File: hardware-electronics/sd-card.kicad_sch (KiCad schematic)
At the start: 48 parts, among them J5 Micro_SD_Card_Det_Hirose_DM3AT, J8 TC2030-IDC-NL, Q6 BSS138, Q7 BSS138, U6 24AA04T-I_OT, U9 USB2244-AEZG-06, Y3 ECS-240-10-47-CKM-TR

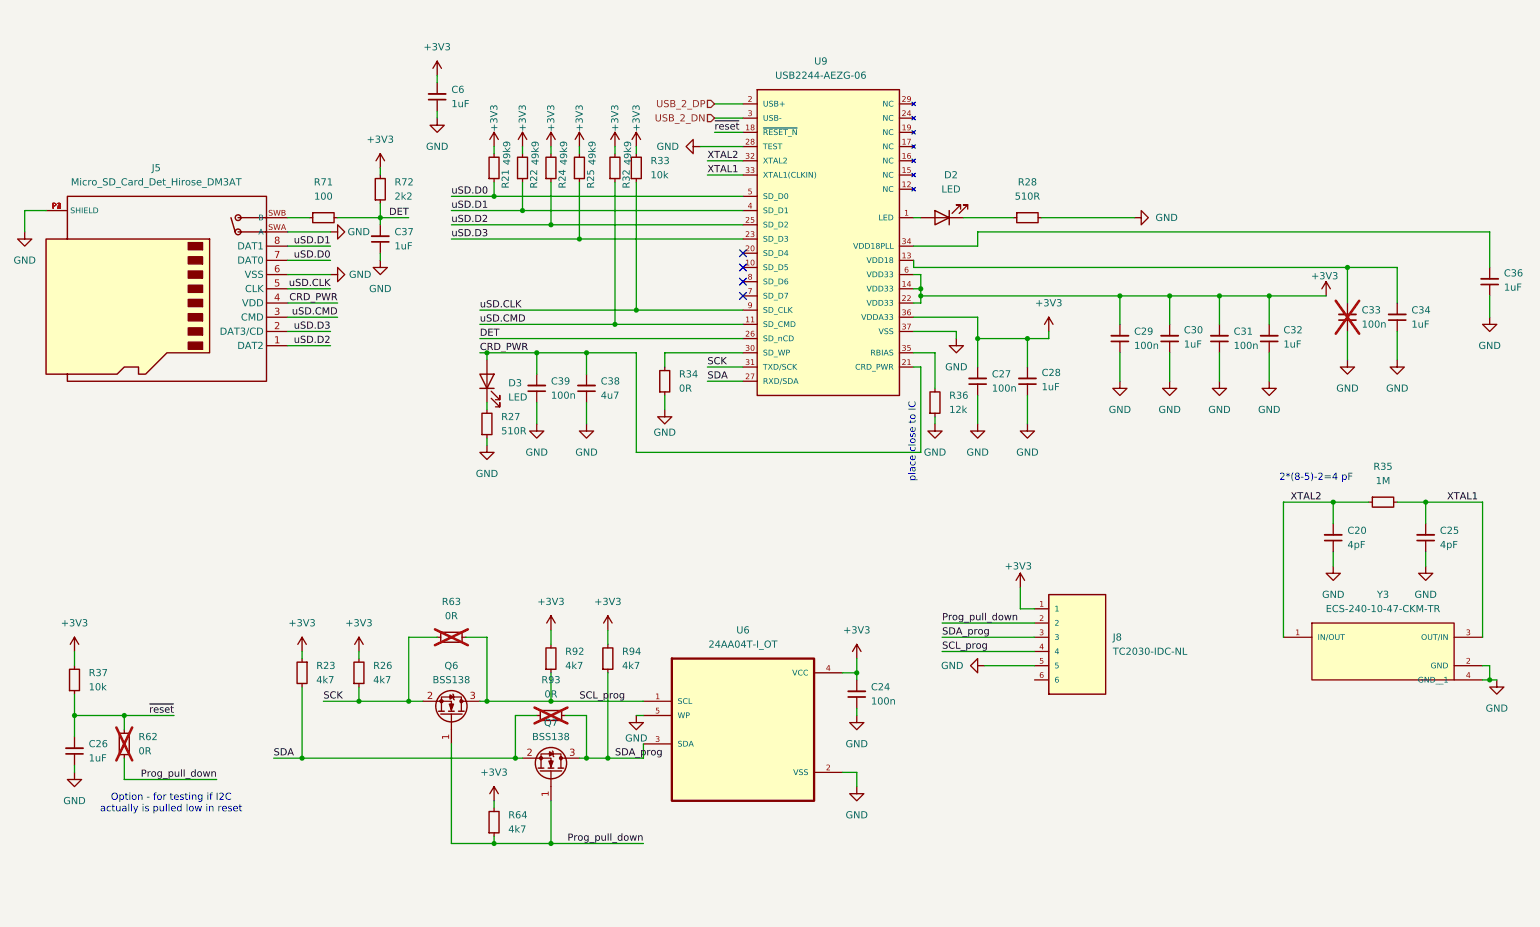
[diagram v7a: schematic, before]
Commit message: Schematic cosmetic changes
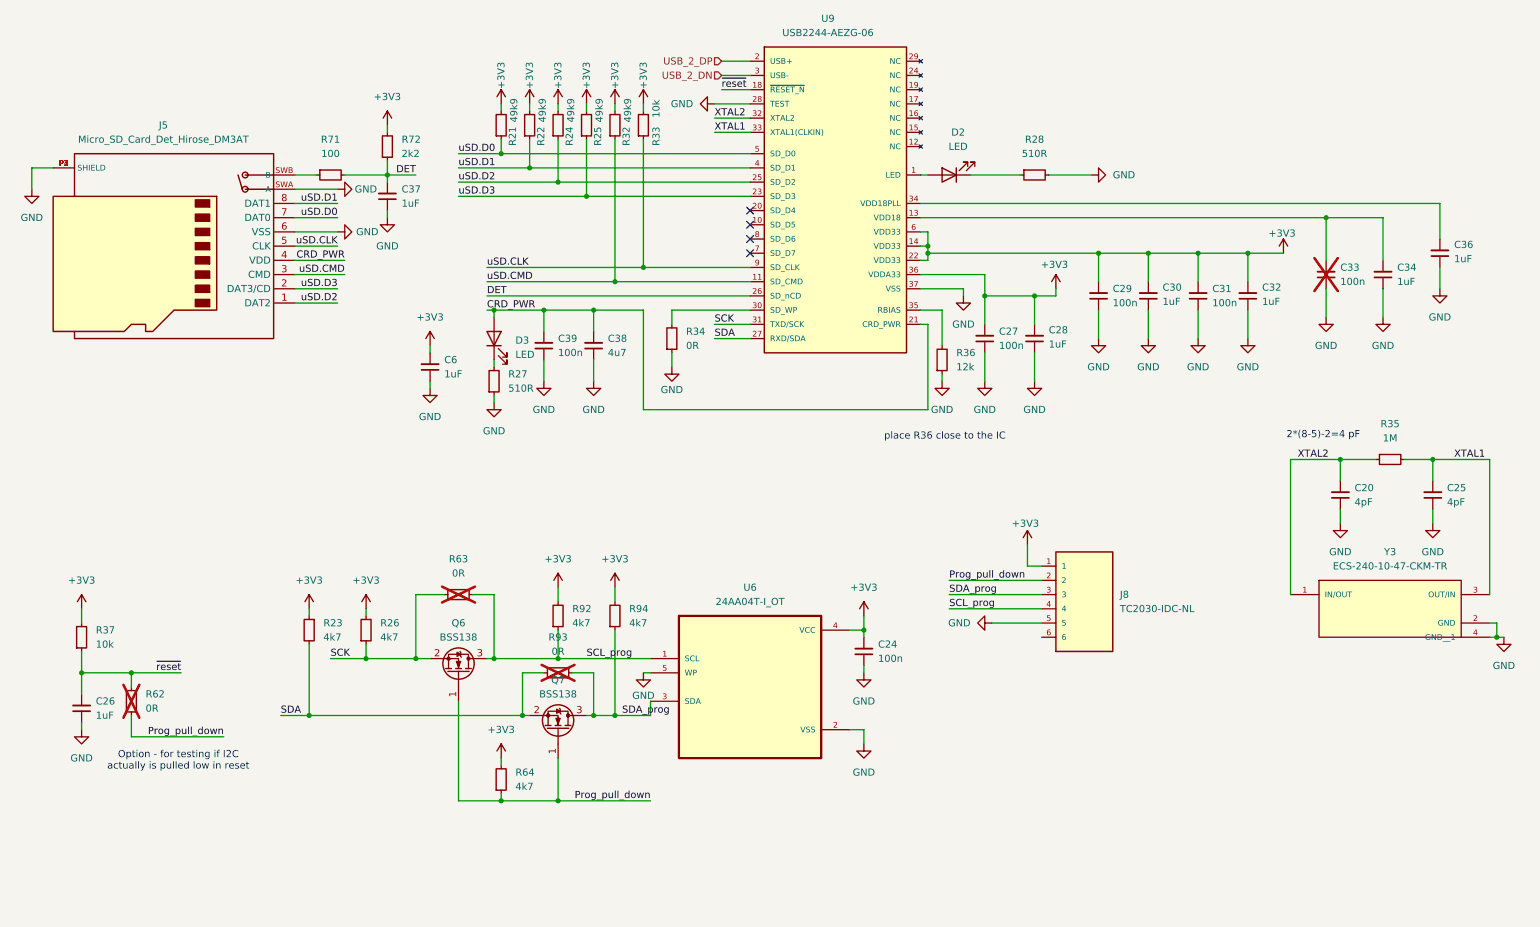
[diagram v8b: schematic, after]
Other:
- note added: "place R36 close to the IC"
- note removed: "place close to IC"
- moved on the sheet: C20, C24, C25, C26, C27, C28, C29, C30, C31, C32, C33, C34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
